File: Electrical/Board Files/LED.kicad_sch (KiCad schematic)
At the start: 0 parts

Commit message: Updating for 3v3 operation
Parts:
- added C? (x2): 1u, symbol Device:C_Small
- added C?: 10u, symbol Device:C_Small
- added D? (x5): WS2812B, LED_SMD:LED_WS2812B_PLCC4_5.0x5.0mm_P3.2mm, symbol LED:WS2812B
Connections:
- new net: D?.1 (VDD), D?.1 (VDD), D?.1 (VDD), D?.1 (VDD), D?.1 (VDD)
- new net: D?.2 (DOUT), D?.4 (DIN) (x4)
- new net +3V3: C?.1, C?.1, C?.1
- new net GND: C?.2, C?.2, C?.2, D?.3 (VSS), D?.3 (VSS), D?.3 (VSS), D?.3 (VSS), D?.3 (VSS)
- new net SPI1.MOSI: D?.4 (DIN)

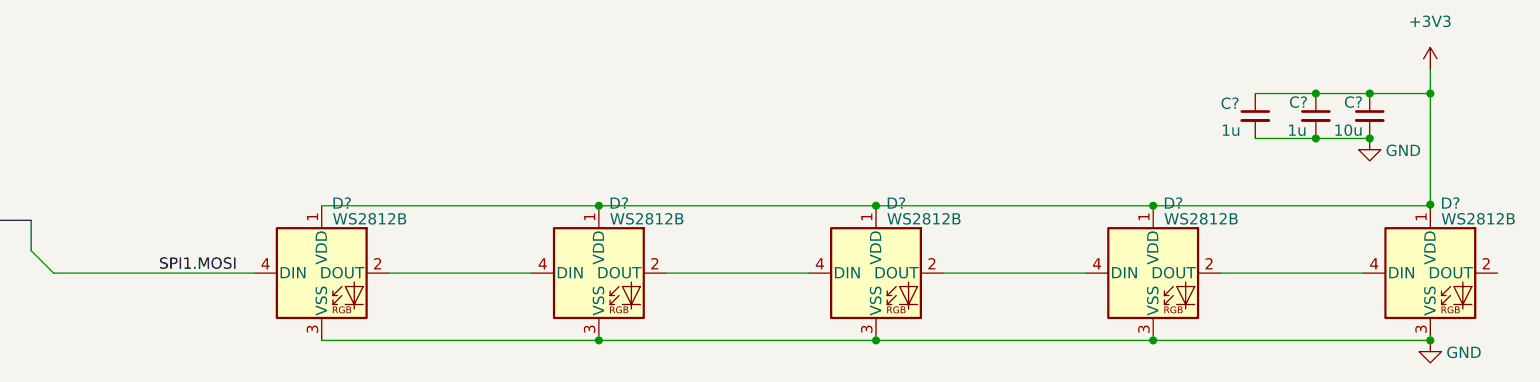
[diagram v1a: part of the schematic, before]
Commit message: Adding power dissipation notes. Removing WS2821B since they won't work with a 3v3 supply
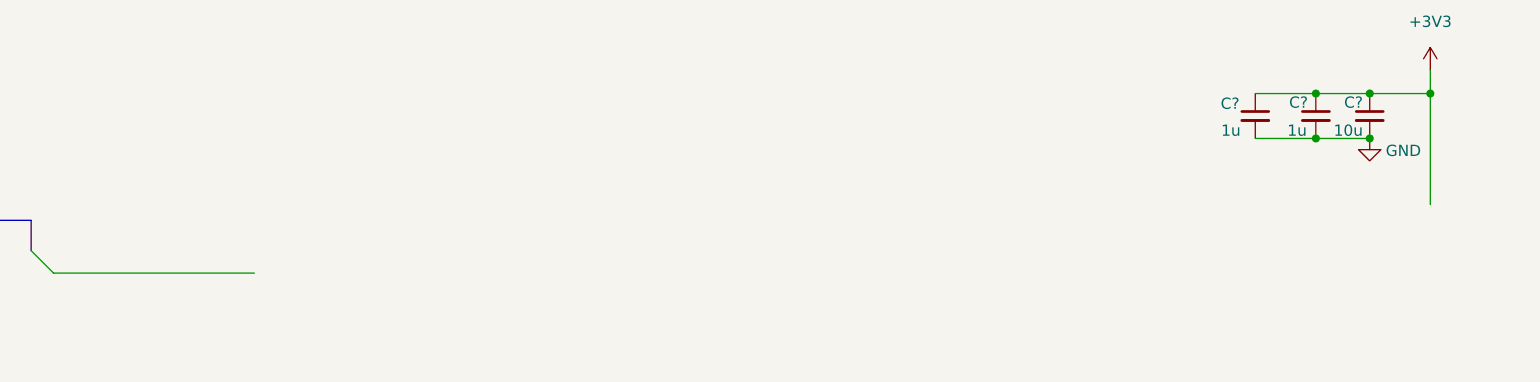
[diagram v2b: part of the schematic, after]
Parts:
- removed D? (x5): WS2812B, LED_SMD:LED_WS2812B_PLCC4_5.0x5.0mm_P3.2mm, symbol LED:WS2812B
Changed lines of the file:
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@@
   (junction (at 222.504 64.008) (diameter 0) (color 0 0 0 0)
   )
-  (junction (at 229.362 71.501) (diameter 0) (color 0 0 0 0)
-  )
-  (junction (at 229.362 86.868) (diameter 0) (color 0 0 0 0)
-  )
-  (junction (at 166.624 71.628) (diameter 0) (color 0 0 0 0)
-  )
-  (junction (at 197.993 86.868) (diameter 0) (color 0 0 0 0)
-  )
-  (junction (at 135.255 71.628) (diameter 0) (color 0 0 0 0)
-  )
   (junction (at 222.504 58.928) (diameter 0) (color 0 0 0 0)
-  )
-  (junction (at 197.993 71.628) (diameter 0) (color 0 0 0 0)
-  )
-  (junction (at 166.624 86.868) (diameter 0) (color 0 0 0 0)
   )
   (junction (at 229.362 58.928) (diameter 0) (color 0 0 0 0)
   )
   (junction (at 216.408 64.008) (diameter 0) (color 0 0 0 0)
-  )
-  (junction (at 135.255 86.868) (diameter 0) (color 0 0 0 0)
   )
   (junction (at 216.408 58.928) (diameter 0) (color 0 0 0 0)
@@
     (stroke (width 0) (type default) (color 0 0 0 0))
   )
-  (wire (pts (xy 166.624 86.868) (xy 197.993 86.868))
-    (stroke (width 0) (type default) (color 0 0 0 0))
-  )
-  (wire (pts (xy 103.886 71.628) (xy 135.255 71.628))
-    (stroke (width 0) (type default) (color 0 0 0 0))
-  )
-  (wire (pts (xy 142.875 79.248) (xy 159.004 79.248))
-    (stroke (width 0) (type default) (color 0 0 0 0))
-  )
   (wire (pts (xy 222.504 58.928) (xy 216.408 58.928))
     (stroke (width 0) (type default) (color 0 0 0 0))
@@
     (stroke (width 0) (type default) (color 0 0 0 0))
   )
-  (wire (pts (xy 135.255 86.868) (xy 166.624 86.868))
-    (stroke (width 0) (type default) (color 0 0 0 0))
-  )
-  (wire (pts (xy 174.244 79.248) (xy 190.373 79.248))
-    (stroke (width 0) (type default) (color 0 0 0 0))
-  )
-  (wire (pts (xy 103.886 86.868) (xy 135.255 86.868))
-    (stroke (width 0) (type default) (color 0 0 0 0))
-  )
   (wire (pts (xy 216.408 64.008) (xy 209.55 64.008))
-    (stroke (width 0) (type default) (color 0 0 0 0))
-  )
-  (wire (pts (xy 111.506 79.248) (xy 127.635 79.248))
     (stroke (width 0) (type default) (color 0 0 0 0))
   )
@@
     (stroke (width 0) (type default) (color 0 0 0 0))
   )
-  (wire (pts (xy 166.624 71.628) (xy 197.993 71.628))
-    (stroke (width 0) (type default) (color 0 0 0 0))
-  )
   (wire (pts (xy 229.362 56.261) (xy 229.362 58.928))
-    (stroke (width 0) (type default) (color 0 0 0 0))
-  )
-  (wire (pts (xy 205.613 79.248) (xy 221.742 79.248))
     (stroke (width 0) (type default) (color 0 0 0 0))
   )
@@
     (stroke (width 0) (type default) (color 0 0 0 0))
   )
-  (wire (pts (xy 197.993 71.628) (xy 229.362 71.628))
-    (stroke (width 0) (type default) (color 0 0 0 0))
-  )
-  (wire (pts (xy 135.255 71.628) (xy 166.624 71.628))
-    (stroke (width 0) (type default) (color 0 0 0 0))
-  )
   (wire (pts (xy 73.533 79.248) (xy 96.266 79.248))
     (stroke (width 0) (type default) (color 0 0 0 0))
-  )
-  (wire (pts (xy 197.993 86.868) (xy 229.362 86.868))
-    (stroke (width 0) (type default) (color 0 0 0 0))
-  )
-  (label "SPI1.MOSI" (at 85.471 79.248 0)
-    (effects (font (size 1.27 1.27)) (justify left bottom))
   )
   (hierarchical_label "SPI1{SCK MISO MOSI}" (shape bidirectional) (at 44.069 73.279 180)
@@
     (pin "1")
   )
-  (symbol (lib_id "LED:WS2812B") (at 135.255 79.248 0) (unit 1)
-    (in_bom yes) (on_board yes)
-    (property "Reference" "D?" (id 0) (at 137.541 71.374 0))
-    (property "Value" "WS2812B" (id 1) (at 140.716 73.152 0))
-    (property "Footprint" "LED_SMD:LED_WS2812B_PLCC4_5.0x5.0mm_P3.2mm" (id 2) (at 136.525 86.868 0)
-      (effects (font (size 1.27 1.27)) (justify left top) hide)
-    )
-    (property "Datasheet" "https://cdn-shop.adafruit.com/datasheets/WS2812B.pdf" (id 3) (at 137.795 88.773 0)
-      (effects (font (size 1.27 1.27)) (justify left top) hide)
-    )
-    (pin "1")
-    (pin "2")
-    (pin "3")
-    (pin "4")
-  )
   (symbol (lib_id "Device:C_Small") (at 216.408 61.468 0) (mirror y) (unit 1)
     (in_bom yes) (on_board yes)
@@
     (pin "1")
     (pin "2")
-  )
-  (symbol (lib_id "LED:WS2812B") (at 166.624 79.248 0) (unit 1)
-    (in_bom yes) (on_board yes)
-    (property "Reference" "D?" (id 0) (at 168.91 71.374 0))
-    (property "Value" "WS2812B" (id 1) (at 172.085 73.152 0))
-    (property "Footprint" "LED_SMD:LED_WS2812B_PLCC4_5.0x5.0mm_P3.2mm" (id 2) (at 167.894 86.868 0)
-      (effects (font (size 1.27 1.27)) (justify left top) hide)
-    )
-    (property "Datasheet" "https://cdn-shop.adafruit.com/datasheets/WS2812B.pdf" (id 3) (at 169.164 88.773 0)
-      (effects (font (size 1.27 1.27)) (justify left top) hide)
-    )
-    (pin "1")
-    (pin "2")
-    (pin "3")
-    (pin "4")
-  )
-  (symbol (lib_id "LED:WS2812B") (at 197.993 79.248 0) (unit 1)
-    (in_bom yes) (on_board yes)
-    (property "Reference" "D?" (id 0) (at 200.279 71.374 0))
-    (property "Value" "WS2812B" (id 1) (at 203.454 73.152 0))
-    (property "Footprint" "LED_SMD:LED_WS2812B_PLCC4_5.0x5.0mm_P3.2mm" (id 2) (at 199.263 86.868 0)
-      (effects (font (size 1.27 1.27)) (justify left top) hide)
-    )
-    (property "Datasheet" "https://cdn-shop.adafruit.com/datasheets/WS2812B.pdf" (id 3) (at 200.533 88.773 0)
-      (effects (font (size 1.27 1.27)) (justify left top) hide)
-    )
-    (pin "1")
-    (pin "2")
-    (pin "3")
-    (pin "4")
   )
   (symbol (lib_id "power:GND") (at 222.504 64.008 0) (unit 1)
@@
     (pin "2")
   )
-  (symbol (lib_id "LED:WS2812B") (at 229.362 79.248 0) (unit 1)
-    (in_bom yes) (on_board yes)
-    (property "Reference" "D?" (id 0) (at 231.648 71.374 0))
-    (property "Value" "WS2812B" (id 1) (at 234.823 73.152 0))
-    (property "Footprint" "LED_SMD:LED_WS2812B_PLCC4_5.0x5.0mm_P3.2mm" (id 2) (at 230.632 86.868 0)
-      (effects (font (size 1.27 1.27)) (justify left top) hide)
-    )
-    (property "Datasheet" "https://cdn-shop.adafruit.com/datasheets/WS2812B.pdf" (id 3) (at 231.902 88.773 0)
-      (effects (font (size 1.27 1.27)) (justify left top) hide)
-    )
-    (pin "1")
-    (pin "2")
-    (pin "3")
-    (pin "4")
-  )
   (symbol (lib_id "Device:C_Small") (at 222.504 61.468 0) (mirror y) (unit 1)
     (in_bom yes) (on_board yes)
@@
     (pin "2")
   )
-  (symbol (lib_id "power:GND") (at 229.362 86.868 0) (unit 1)
-    (in_bom yes) (on_board yes)
-    (property "Reference" "#PWR?" (id 0) (at 229.362 93.218 0)
-      (effects (font (size 1.27 1.27)) hide)
-    )
-    (property "Value" "GND" (id 1) (at 233.172 88.265 0))
-    (property "Footprint" "" (id 2) (at 229.362 86.868 0)
-      (effects (font (size 1.27 1.27)) hide)
-    )
-    (property "Datasheet" "" (id 3) (at 229.362 86.868 0)
-      (effects (font (size 1.27 1.27)) hide)
-    )
-    (pin "1")
-  )
-  (symbol (lib_id "LED:WS2812B") (at 103.886 79.248 0) (unit 1)
-    (in_bom yes) (on_board yes)
-    (property "Reference" "D?" (id 0) (at 106.172 71.374 0))
-    (property "Value" "WS2812B" (id 1) (at 109.347 73.152 0))
-    (property "Footprint" "LED_SMD:LED_WS2812B_PLCC4_5.0x5.0mm_P3.2mm" (id 2) (at 105.156 86.868 0)
-      (effects (font (size 1.27 1.27)) (justify left top) hide)
-    )
-    (property "Datasheet" "https://cdn-shop.adafruit.com/datasheets/WS2812B.pdf" (id 3) (at 106.426 88.773 0)
-      (effects (font (size 1.27 1.27)) (justify left top) hide)
-    )
-    (pin "1")
-    (pin "2")
-    (pin "3")
-    (pin "4")
-  )
 )

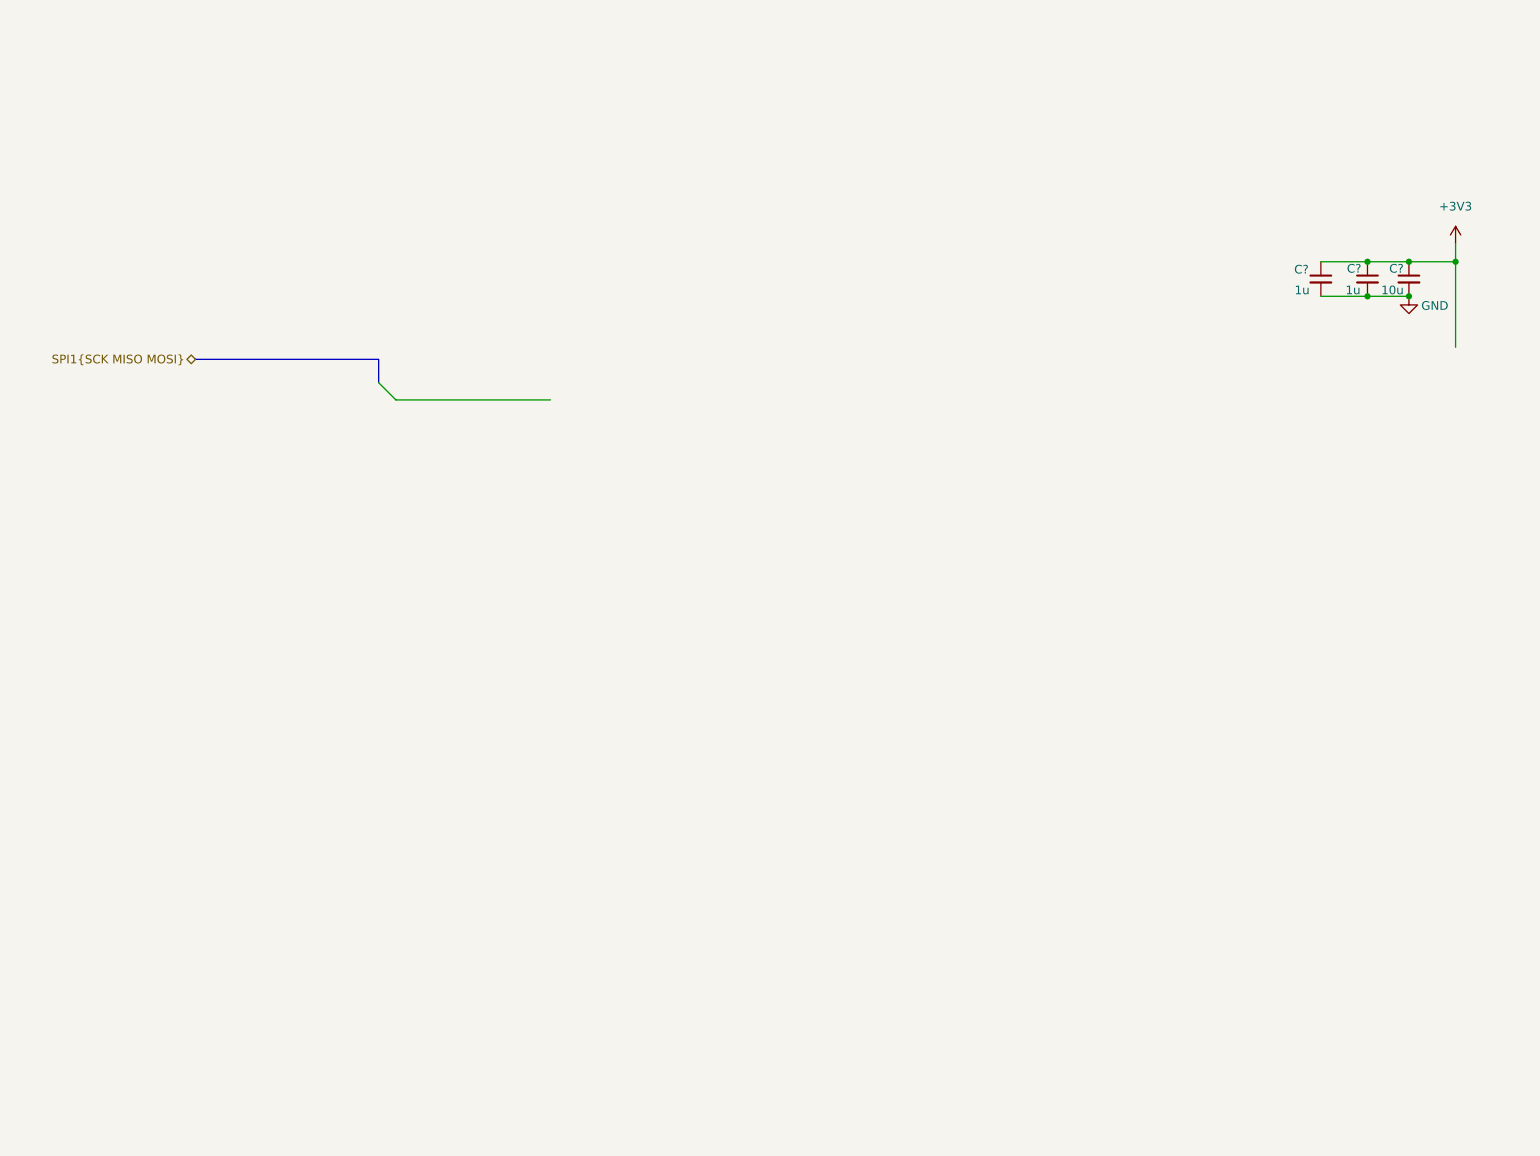
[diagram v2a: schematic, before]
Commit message: Added buzz and vibe, moved SPI, added 2 LEDs
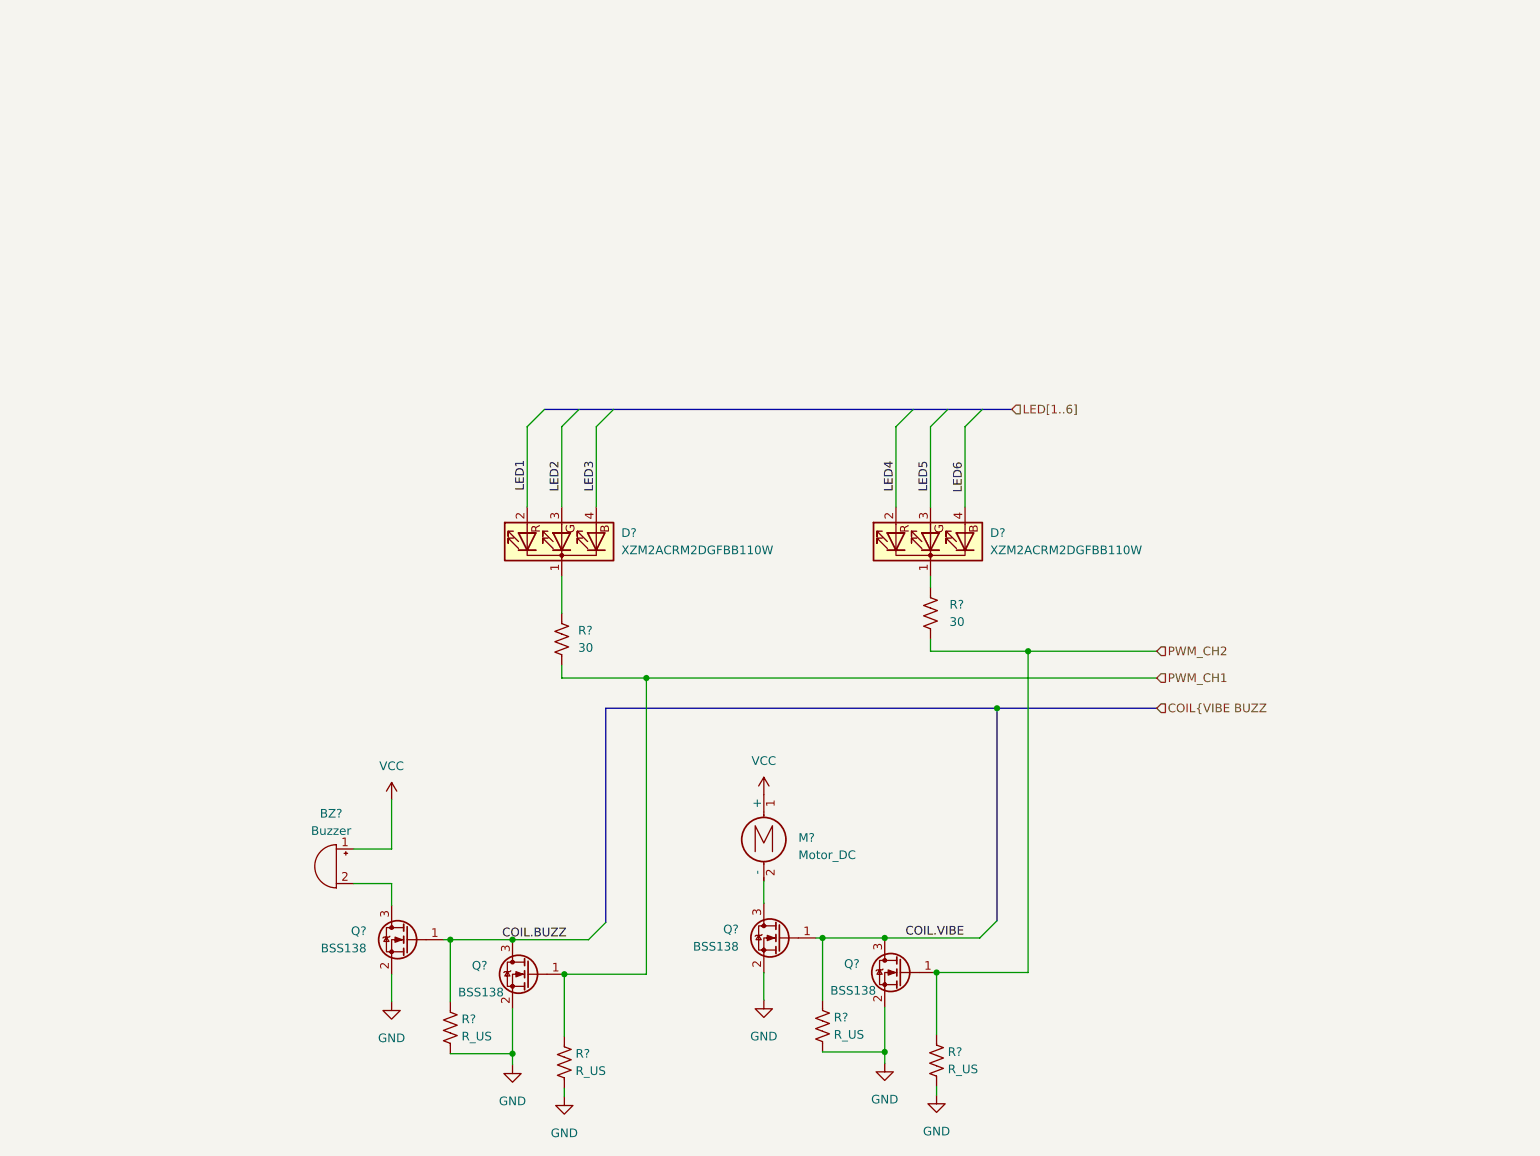
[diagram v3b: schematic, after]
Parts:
- removed C? (x2): 1u, symbol Device:C_Small
- removed C?: 10u, symbol Device:C_Small
- added BZ?: Buzzer, symbol Device:Buzzer
- added D? (x2): XZM2ACRM2DGFBB110W, symbol Device:LED_KRGB
- added M?: Motor_DC, symbol Motor:Motor_DC
- added Q? (x4): BSS138, Package_TO_SOT_SMD:SOT-23, symbol Transistor_FET:BSS138
- added R? (x4): R_US, symbol Device:R_US
- added R? (x2): 30, symbol Device:R_US
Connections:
- net GND: now also Q?.2 (S), Q?.2 (S), Q?.2 (S), Q?.2 (S), R?.2, R?.2, R?.2, R?.2
- new net: M?.2 (-), Q?.3 (D)
- new net: BZ?.2 (+), Q?.3 (D)
- new net: D?.1 (K), R?.1 (x2)
- new net COIL.BUZZ: Q?.1 (G), Q?.3 (D), R?.1
- new net COIL.VIBE: Q?.1 (G), Q?.3 (D), R?.1
- new net LED1: D?.2 (RA)
- new net LED2: D?.3 (GA)
- new net LED3: D?.4 (BA)
- new net LED4: D?.2 (RA)
- new net LED5: D?.3 (GA)
- new net LED6: D?.4 (BA)
- new net PWM_CH1: Q?.1 (G), R?.1, R?.2
- new net PWM_CH2: Q?.1 (G), R?.1, R?.2
- new net VCC: BZ?.1 (-), M?.1 (+)

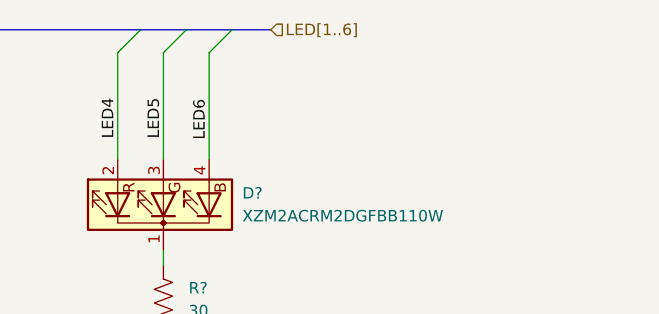
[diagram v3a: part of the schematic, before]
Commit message: Updating sheet template
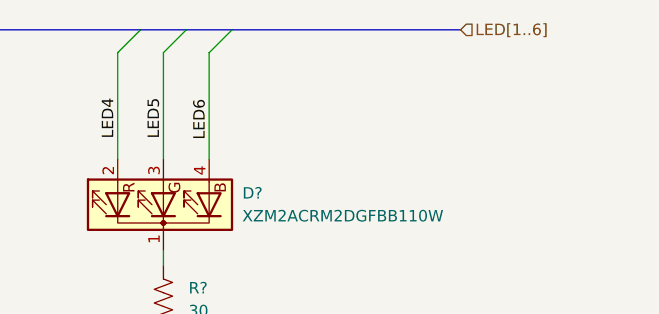
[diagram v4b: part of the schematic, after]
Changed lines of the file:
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@@
     (stroke (width 0) (type default) (color 0 0 0 0))
   )
-  (bus (pts (xy 159.766 80.645) (xy 164.084 80.645))
+  (bus (pts (xy 159.766 80.645) (xy 185.166 80.645))
     (stroke (width 0) (type default) (color 0 0 0 0))
   )
@@
     (effects (font (size 1.27 1.27)) (justify left))
   )
-  (hierarchical_label "LED[1..6]" (shape input) (at 164.084 80.645 0)
+  (hierarchical_label "LED[1..6]" (shape input) (at 185.166 80.645 0)
     (effects (font (size 1.27 1.27)) (justify left))
   )

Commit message: Added Xbee libs and bus aliases
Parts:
- added Q4, Q7: BSS138, Package_TO_SOT_SMD:SOT-23, symbol Transistor_FET:BSS138
- added R11, R17: 100, symbol Device:R_US
- added R12, R18: 10k, symbol Device:R_US
- added R13, R19: 1k, symbol Device:R_US
- R16, R20: renamed from R?; value R_US -> 10k
- gave numbers to parts that had none: 12
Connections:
- net COIL.BUZZ: now also R13.2; no longer Q3.1 (G), Q5.3 (D), R10.1
- net COIL.VIBE: now also R19.2; no longer Q6.1 (G), Q8.3 (D), R16.1
- net GND: now also Q4.2 (S), Q7.2 (S), R12.2, R18.2
- net PWM_CH1: now also R11.2, R12.1; no longer R9.2
- net PWM_CH2: now also R17.2, R18.1; no longer R15.2
- new net: Q7.1 (G), R17.1
- new net: Q7.3 (D), R15.2
- new net: Q3.1 (G), Q5.3 (D), R10.1, R13.1
- new net: Q6.1 (G), Q8.3 (D), R16.1, R19.1
- new net: Q4.3 (D), R9.2
- new net: Q4.1 (G), R11.1
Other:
- title: (none) -> Robotics Controller
- moved on the sheet: BZ1, D17, D18, M1, Q3, Q5, Q6, Q8, R10, R14, R15, R16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

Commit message: Updating title block fields and adding pdf schematic
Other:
- company: (none) -> Rockerbotics
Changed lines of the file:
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@@
   (title_block
     (title "Robotics Controller")
+    (date "2022-09-02")
     (rev "A")
+    (company "Rockerbotics")
   )
   (junction (at 55.626 146.304) (diameter 0) (color 0 0 0 0)
